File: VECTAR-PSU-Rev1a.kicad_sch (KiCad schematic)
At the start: 63 parts, among them J1 XT60PW-M, J2 XT60PW-M, J3 Conn_01x02_Socket, J5 Conn_01x06_Socket, J6 XT90PW-M, Q1 2N7002, Q2 IRFB7437, Q3 IRFB7437, SW2 RA1113112R, U1 LM74502DDFR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

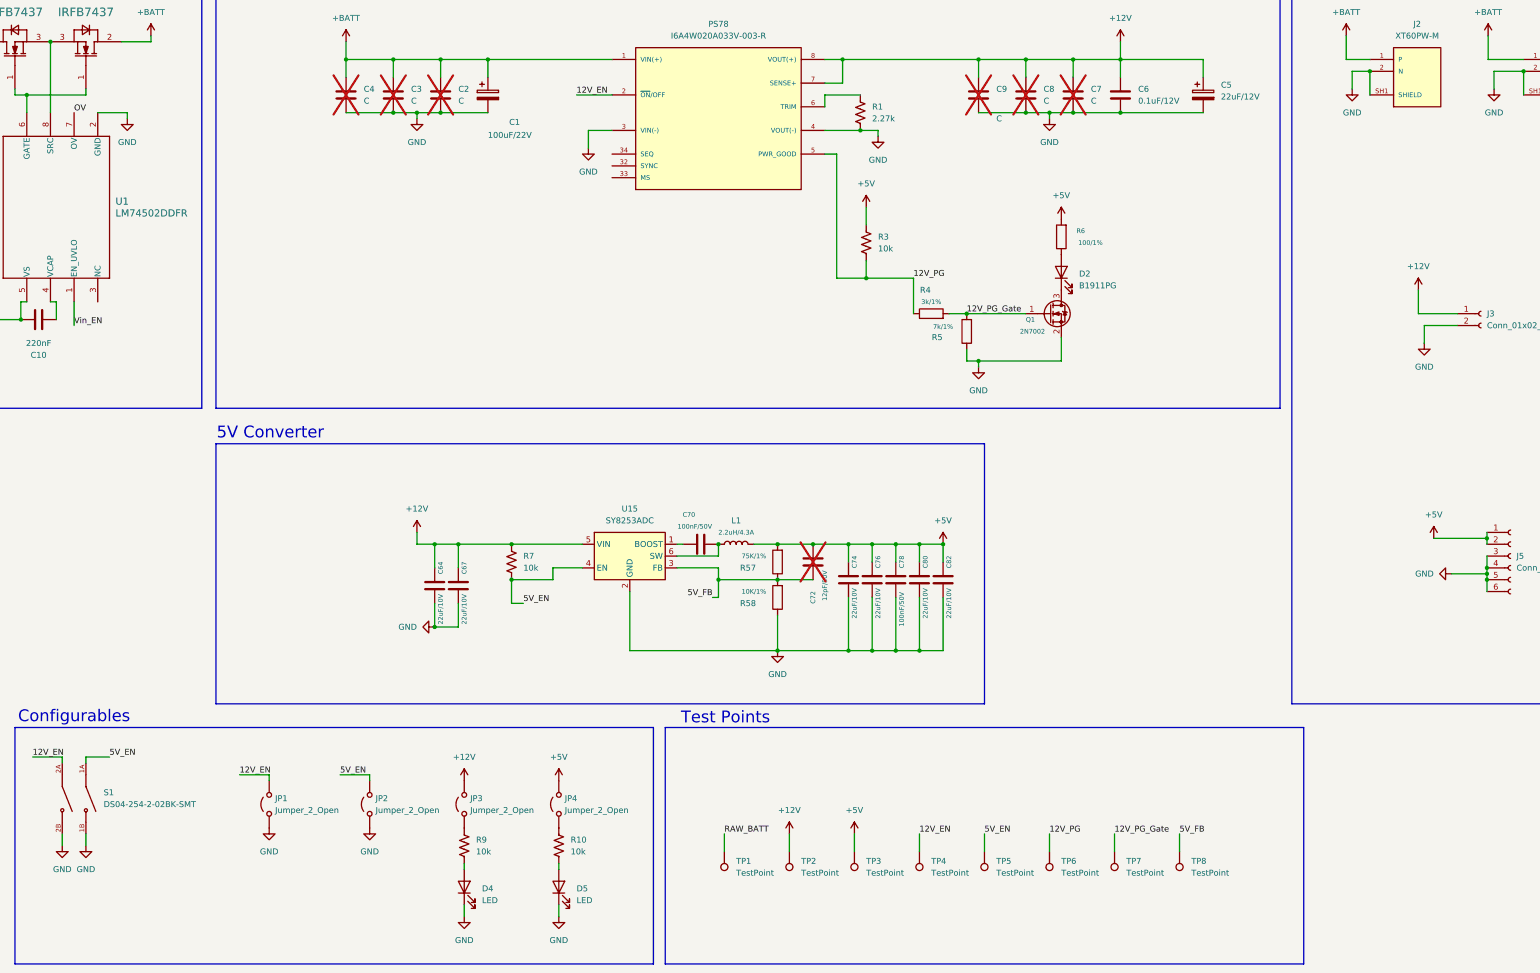
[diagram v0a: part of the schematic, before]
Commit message: schematic complete, adding footprints now
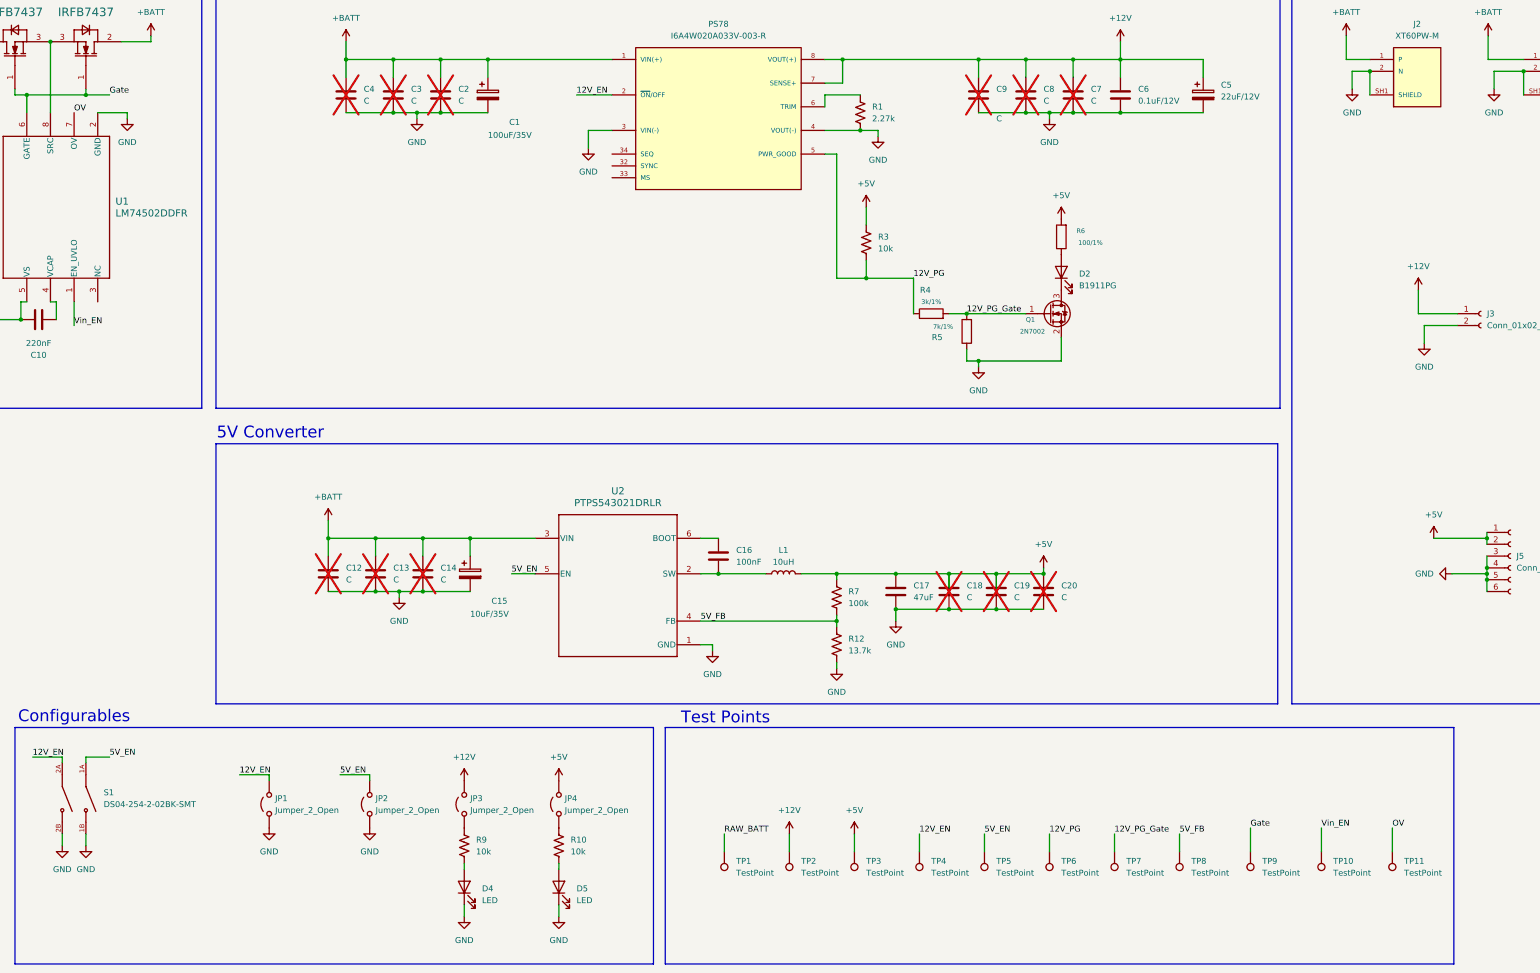
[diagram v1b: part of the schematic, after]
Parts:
- removed C64, C67, C74, C76, C80, C82: 22uF/10V, Capacitor_SMD:C_0603_1608Metric, symbol Device:C
- removed C70, C78: 100nF/50V, Capacitor_SMD:C_0603_1608Metric, symbol Device:C
- removed C72: 12pF/50V, Capacitor_SMD:C_0402_1005Metric, symbol Device:C
- removed R57: 75K/1%, Resistor_SMD:R_0603_1608Metric, symbol Device:R
- removed R58: 10K/1%, Resistor_SMD:R_0603_1608Metric, symbol Device:R
- removed U15: SY8253ADC, symbol Regulator_Switching:LM2734X
- added C12, C13, C14, C18, C19, C20: C, Capacitor_SMD:C_0603_1608Metric, symbol Device:C
- added C15: 10uF/35V, Capacitor_SMD:C_0603_1608Metric, symbol Device:C_Polarized
- added C16: 100nF, Capacitor_SMD:C_0603_1608Metric, symbol Device:C
- added C17: 47uF, PSU-Rev1:CAPAE660X600N, symbol Device:C
- added R12: 13.7k, Resistor_SMD:R_0603_1608Metric, symbol Device:R_US
- added TP10, TP11, TP9: TestPoint, symbol Connector:TestPoint
- added U2: PTPS543021DRLR, PSU-Rev1:DRL0006A-MFG, symbol PSU-Rev1:PTPS543021DRLR
- C1: value 100uF/22V -> 100uF/35V; footprint (none) -> PSU-Rev1:EHBSA035M1010608T
- C5: footprint (none) -> Capacitor_SMD:C_0805_2012Metric
- F1: footprint (none) -> PSU-Rev1:0498150.M
- L1: value 2.2uH/4.3A -> 10uH; footprint (none) -> PSU-Rev1:IND_BOURNS_SDR1307
- Q1: footprint (none) -> PSU-Rev1:SOT95P240X111-3N
- Q2, Q3: footprint (none) -> Resistor_SMD:R_0603_1608Metric
- R7: value 10k -> 100k
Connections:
- net +12V: no longer R7.1
- net +5V: now also R7.1, C17.1, C18.1, C19.1, C20.1
- net +BATT: now also C12.1, C13.1, C14.1, C15.1, U2.3 (VIN)
- net 5V_EN: now also U2.5 (EN); no longer R7.2
- net 5V_FB: now also R7.2, R12.1, U2.4 (FB)
- net GND: now also C12.2, C13.2, C14.2, C15.2, C17.2, C18.2, C19.2, C20.2, R12.2, U2.1 (GND)
- net OV: now also TP11.1
- net Vin_EN: now also TP10.1
- net Gate: now reaches Q2.1 (GATE), Q3.1 (GATE), U1.6 (GATE)
- net Gate: now also TP9.1
- net at L1.1: now also C16.2, U2.2 (SW)
- new net: C16.1, U2.6 (BOOT)

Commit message: schematic complete, layout started
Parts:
- D4: value LED -> Yellow; footprint (none) -> PSU-Rev1:LTST_C190KSKT
- D5: value LED -> Red; footprint (none) -> PSU-Rev1:LTST_S270KRKT
- J3: footprint PSU-Rev1:AMASS_XT60PW-M -> PSU-Rev1:Rocker-Switch
- J5: footprint (none) -> PSU-Rev1:6-pin-connector
- JP1, JP2, JP3, JP4: footprint (none) -> Resistor_SMD:R_0603_1608Metric
- Q2, Q3: footprint Resistor_SMD:R_0603_1608Metric -> PSU-Rev1:TO254P483X1016X1944-3B
- R1: footprint Resistor_SMD:R_0603_1608Metric -> Resistor_SMD:R_0805_2012Metric
- R10: value 10k -> 150
- R9: value 10k -> 500
- SW2: footprint (none) -> PSU-Rev1:Rocker-Switch
- TP1, TP10, TP11, TP2, TP3, TP4, TP5, TP6, TP7, TP8, TP9: footprint (none) -> PSU-Rev1:KEYSTONE_5002
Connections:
- net GND: now also J6.2 (NEG), J6.S1, J6.S2; no longer J6.N (NEG)
- net RAW_BATT: now also J6.1 (POS); no longer J6.P (POS)
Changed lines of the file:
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@@
 	)
 	(junction
+		(at 107.95 88.9)
+		(diameter 0)
+		(color 0 0 0 0)
+	)
+	(junction
 		(at 353.06 203.2)
 		(diameter 0)
@@
 	)
 	(junction
+		(at 93.98 91.44)
+		(diameter 0)
+		(color 0 0 0 0)
+	)
+	(junction
 		(at 102.87 118.11)
 		(diameter 0)
@@
 	(wire
 		(pts
+			(xy 105.41 88.9) (xy 107.95 88.9)
+		)
+		(stroke
+			(width 0)
+			(type default)
+		)
+	)
+	(wire
+		(pts
 			(xy 144.78 92.71) (xy 144.78 96.52)
 		)
@@
 	(wire
 		(pts
+			(xy 90.17 73.66) (xy 90.17 91.44)
+		)
+		(stroke
+			(width 0)
+			(type default)
+		)
+	)
+	(wire
+		(pts
 			(xy 152.4 251.46) (xy 152.4 254)
 		)
@@
 	(wire
 		(pts
+			(xy 90.17 91.44) (xy 93.98 91.44)
+		)
+		(stroke
+			(width 0)
+			(type default)
+		)
+	)
+	(wire
+		(pts
 			(xy 243.84 85.09) (xy 270.51 85.09)
 		)
@@
 	(wire
 		(pts
+			(xy 93.98 91.44) (xy 105.41 91.44)
+		)
+		(stroke
+			(width 0)
+			(type default)
+		)
+	)
+	(wire
+		(pts
 			(xy 350.52 251.46) (xy 350.52 255.27)
 		)
@@
 	(wire
 		(pts
+			(xy 93.98 73.66) (xy 90.17 73.66)
+		)
+		(stroke
+			(width 0)
+			(type default)
+		)
+	)
+	(wire
+		(pts
 			(xy 316.23 100.33) (xy 323.85 100.33)
 		)
@@
 	(wire
 		(pts
+			(xy 105.41 91.44) (xy 105.41 88.9)
+		)
+		(stroke
+			(width 0)
+			(type default)
+		)
+	)
+	(wire
+		(pts
 			(xy 342.9 195.58) (xy 342.9 199.39)
 		)
@@
 			)
 		)
-		(property "Footprint" ""
+		(property "Footprint" "PSU-Rev1:KEYSTONE_5002"
 			(at 373.38 255.27 0)
 			(effects
@@
 			)
 		)
-		(property "Footprint" ""
+		(property "Footprint" "Resistor_SMD:R_0603_1608Metric"
 			(at 218.44 245.11 0)
 			(effects
@@
 			)
 		)
-		(property "Footprint" "Resistor_SMD:R_0603_1608Metric"
+		(property "Footprint" "PSU-Rev1:TO254P483X1016X1944-3B"
 			(at 139.7 86.36 0)
 			(effects
@@
 			)
 		)
-		(property "Footprint" "PSU-Rev1:AMASS_XT60PW-M"
+		(property "Footprint" "PSU-Rev1:Rocker-Switch"
 			(at 457.2 139.7 0)
 			(effects
@@
 			)
 		)
-		(property "Value" "10k"
+		(property "Value" "500"
 			(at 241.3 255.2699 0)
 			(effects
@@
 			)
 		)
-		(property "Footprint" ""
+		(property "Footprint" "Resistor_SMD:R_0603_1608Metric"
 			(at 196.85 245.11 0)
 			(effects
@@
 			)
 		)
-		(property "Value" "10k"
+		(property "Value" "150"
 			(at 261.62 255.2699 0)
 			(effects
@@
 			)
 		)
-		(pin "P"
+		(pin "S1"
+		)
+		(pin "S2"
 		)
-		(pin "N"
+		(pin "1"
+		)
+		(pin "2"
 		)
 		(instances
@@
 			)
 		)
-		(property "Footprint" "Resistor_SMD:R_0603_1608Metric"
+		(property "Footprint" "Resistor_SMD:R_0805_2012Metric"
 			(at 324.866 96.774 90)
 			(effects
@@
 			)
 		)
-		(property "Footprint" ""
+		(property "Footprint" "PSU-Rev1:KEYSTONE_5002"
 			(at 402.59 255.27 0)
 			(effects
@@
 			)
 		)
-		(property "Value" "LED"
+		(property "Value" "Yellow"
 			(at 242.57 265.7474 90)
 			(effects
@@
 			)
 		)
-		(property "Footprint" ""
+		(property "Footprint" "PSU-Rev1:LTST_C190KSKT"
 			(at 238.76 262.89 0)
 			(effects
@@
 			)
 		)
-		(property "Datasheet" "~"
+		(property "Datasheet" "https://optoelectronics.liteon.com/upload/download/DS-22-99-0189/LTST-C190KSKT.pdf"
 			(at 238.76 262.89 0)
 			(effects
@@
 			)
 		)
-		(property "Description" "Light emitting diode"
+		(property "Description" "Yellow light emitting diode"
 			(at 238.76 262.89 0)
 			(effects
@@
 			)
 		)
+		(property "Field6" ""
+			(at 238.76 262.89 90)
+			(effects
+				(font
+					(size 1.27 1.27)
+				)
+				(hide yes)
+			)
+		)
+		(property "Field7" ""
+			(at 238.76 262.89 90)
+			(effects
+				(font
+					(size 1.27 1.27)
+				)
+				(hide yes)
+			)
+		)
+		(property "Field8" ""
+			(at 238.76 262.89 90)
+			(effects
+				(font
+					(size 1.27 1.27)
+				)
+				(hide yes)
+			)
+		)
 		(pin "2"
 		)
@@
 			)
 		)
-		(property "Footprint" ""
+		(property "Footprint" "PSU-Rev1:KEYSTONE_5002"
 			(at 345.44 255.27 0)
 			(effects
@@
 			)
 		)
-		(property "Footprint" ""
+		(property "Footprint" "PSU-Rev1:KEYSTONE_5002"
 			(at 331.47 255.27 0)
 			(effects
@@
 			)
 		)
-		(property "Footprint" ""
+		(property "Footprint" "Resistor_SMD:R_0603_1608Metric"
 			(at 259.08 245.11 0)
 			(effects
@@
 			)
 		)
-		(property "Footprint" ""
+		(property "Footprint" "PSU-Rev1:KEYSTONE_5002"
 			(at 433.07 255.27 0)
 			(effects
@@
 			)
 		)
-		(property "Footprint" "Resistor_SMD:R_0603_1608Metric"
+		(property "Footprint" "PSU-Rev1:TO254P483X1016X1944-3B"
 			(at 160.02 86.36 0)
 			(effects
@@
 			)
 		)
-		(property "Footprint" ""
+		(property "Footprint" "PSU-Rev1:6-pin-connector"
 			(at 463.55 191.77 0)
 			(effects
@@
 			)
 		)
-		(property "Footprint" ""
+		(property "Footprint" "PSU-Rev1:KEYSTONE_5002"
 			(at 303.53 255.27 0)
 			(effects
@@
 			)
 		)
-		(property "Footprint" ""
+		(property "Footprint" "PSU-Rev1:KEYSTONE_5002"
 			(at 387.35 255.27 0)
 			(effects
@@
 			)
 		)
-		(property "Footprint" ""
+		(property "Footprint" "PSU-Rev1:KEYSTONE_5002"
 			(at 359.41 255.27 0)
 			(effects
@@
 			)
 		)
-		(property "Footprint" ""
+		(property "Footprint" "PSU-Rev1:KEYSTONE_5002"
 			(at 289.56 255.27 0)
 			(effects
@@
 			)
 		)
-		(property "Footprint" ""
+		(property "Footprint" "PSU-Rev1:KEYSTONE_5002"
 			(at 417.83 255.27 0)
 			(effects
@@
 			)
 		)
-		(property "Footprint" ""
+		(property "Footprint" "Resistor_SMD:R_0603_1608Metric"
 			(at 238.76 245.11 0)
 			(effects
@@
 			)
 		)
-		(property "Footprint" ""
+		(property "Footprint" "PSU-Rev1:KEYSTONE_5002"
 			(at 317.5 255.27 0)
 			(effects
@@
 			)
 		)
-		(property "Value" "LED"
+		(property "Value" "Red"
 			(at 262.89 265.7474 90)
 			(effects
@@
 			)
 		)
-		(property "Footprint" ""
+		(property "Footprint" "PSU-Rev1:LTST_S270KRKT"
 			(at 259.08 262.89 0)
 			(effects
@@
 			)
 		)
-		(property "Datasheet" "~"
+		(property "Datasheet" "https://optoelectronics.liteon.com/upload/download/DS22-2000-210/LTST-S270KRKT.pdf"
 			(at 259.08 262.89 0)
 			(effects
@@
 			)
 		)
-		(property "Footprint" ""
+		(property "Footprint" "PSU-Rev1:Rocker-Switch"
 			(at 121.92 124.46 0)
 			(effects

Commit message: PCB Rev 1 Complete
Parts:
- added TP12: TestPoint, PSU-Rev1:KEYSTONE_5002, symbol Connector:TestPoint
- F1: footprint PSU-Rev1:0498150.M -> PSU-Rev1:3-140-178
- R1: value 2.27k -> 1.9k
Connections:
- net +12V: now also C12.1, C13.1, C14.1, C15.1, U2.1 (VIN)
- net +BATT: no longer C12.1, C13.1, C14.1, C15.1, U2.3 (VIN)
- net 5V_FB: now also U2.6 (FB); no longer U2.4 (FB)
- net GND: now also U2.3 (GND), TP12.1; no longer U2.1 (GND)
- net at C16.1: now also U2.4 (BOOT); no longer U2.6 (BOOT)
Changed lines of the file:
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@@
 	(rectangle
 		(start 281.94 228.6)
-		(end 451.358 279.4)
+		(end 465.328 279.4)
 		(stroke
 			(width 0)
@@
 	(wire
 		(pts
+			(xy 459.74 245.11) (xy 459.74 246.38)
+		)
+		(stroke
+			(width 0)
+			(type default)
+		)
+	)
+	(wire
+		(pts
 			(xy 359.41 85.09) (xy 349.25 85.09)
 		)
@@
 	(wire
 		(pts
+			(xy 453.39 245.11) (xy 453.39 255.27)
+		)
+		(stroke
+			(width 0)
+			(type default)
+		)
+	)
+	(wire
+		(pts
 			(xy 196.85 240.03) (xy 196.85 238.76)
 		)
@@
 	(wire
 		(pts
+			(xy 453.39 245.11) (xy 459.74 245.11)
+		)
+		(stroke
+			(width 0)
+			(type default)
+		)
+	)
+	(wire
+		(pts
 			(xy 318.77 214.63) (xy 318.77 215.9)
 		)
@@
 	)
 	(symbol
-		(lib_id "power:+BATT")
-		(at 209.55 184.15 0)
-		(unit 1)
-		(exclude_from_sim no)
-		(in_bom yes)
-		(on_board yes)
-		(dnp no)
-		(fields_autoplaced yes)
-		(property "Reference" "#PWR08"
-			(at 209.55 187.96 0)
-			(effects
-				(font
-					(size 1.27 1.27)
-				)
-				(hide yes)
-			)
-		)
-		(property "Value" "+BATT"
-			(at 209.55 179.07 0)
-			(effects
-				(font
-					(size 1.27 1.27)
-				)
-			)
-		)
-		(property "Footprint" ""
-			(at 209.55 184.15 0)
-			(effects
-				(font
-					(size 1.27 1.27)
-				)
-				(hide yes)
-			)
-		)
-		(property "Datasheet" ""
-			(at 209.55 184.15 0)
-			(effects
-				(font
-					(size 1.27 1.27)
-				)
-				(hide yes)
-			)
-		)
-		(property "Description" "Power symbol creates a global label with name \"+BATT\""
-			(at 209.55 184.15 0)
-			(effects
-				(font
-					(size 1.27 1.27)
-				)
-				(hide yes)
-			)
-		)
-		(pin "1"
-		)
-		(instances
-			(project "VECTAR-PSU-Rev1a"
-				(path "/4bea2110-1f4a-4734-955b-ccea5d17fc20"
-					(reference "#PWR08")
-					(unit 1)
-				)
-			)
-		)
-	)
-	(symbol
 		(lib_id "PSU-Rev1:XT60PW-M")
 		(at 443.484 87.63 0)
@@
 	)
 	(symbol
+		(lib_id "power:+12V")
+		(at 209.55 184.15 0)
+		(unit 1)
+		(exclude_from_sim no)
+		(in_bom yes)
+		(on_board yes)
+		(dnp no)
+		(fields_autoplaced yes)
+		(property "Reference" "#PWR08"
+			(at 209.55 187.96 0)
+			(effects
+				(font
+					(size 1.27 1.27)
+				)
+				(hide yes)
+			)
+		)
+		(property "Value" "+12V"
+			(at 209.55 179.07 0)
+			(effects
+				(font
+					(size 1.27 1.27)
+				)
+			)
+		)
+		(property "Footprint" ""
+			(at 209.55 184.15 0)
+			(effects
+				(font
+					(size 1.27 1.27)
+				)
+				(hide yes)
+			)
+		)
+		(property "Datasheet" ""
+			(at 209.55 184.15 0)
+			(effects
+				(font
+					(size 1.27 1.27)
+				)
+				(hide yes)
+			)
+		)
+		(property "Description" "Power symbol creates a global label with name \"+12V\""
+			(at 209.55 184.15 0)
+			(effects
+				(font
+					(size 1.27 1.27)
+				)
+				(hide yes)
+			)
+		)
+		(pin "1"
+		)
+		(instances
+			(project "VECTAR-PSU-Rev1a"
+				(path "/4bea2110-1f4a-4734-955b-ccea5d17fc20"
+					(reference "#PWR08")
+					(unit 1)
+				)
+			)
+		)
+	)
+	(symbol
 		(lib_id "power:GND")
 		(at 218.44 250.19 0)
@@
 			)
 		)
-		(property "Value" "2.27k"
+		(property "Value" "1.9k"
 			(at 326.39 97.7899 0)
 			(effects
@@
 	)
 	(symbol
+		(lib_id "power:GND")
+		(at 459.74 246.38 0)
+		(unit 1)
+		(exclude_from_sim no)
+		(in_bom yes)
+		(on_board yes)
+		(dnp no)
+		(fields_autoplaced yes)
+		(property "Reference" "#PWR034"
+			(at 459.74 252.73 0)
+			(effects
+				(font
+					(size 1.27 1.27)
+				)
+				(hide yes)
+			)
+		)
+		(property "Value" "GND"
+			(at 459.74 251.46 0)
+			(effects
+				(font
+					(size 1.27 1.27)
+				)
+			)
+		)
+		(property "Footprint" ""
+			(at 459.74 246.38 0)
+			(effects
+				(font
+					(size 1.27 1.27)
+				)
+				(hide yes)
+			)
+		)
+		(property "Datasheet" ""
+			(at 459.74 246.38 0)
+			(effects
+				(font
+					(size 1.27 1.27)
+				)
+				(hide yes)
+			)
+		)
+		(property "Description" ""
+			(at 459.74 246.38 0)
+			(effects
+				(font
+					(size 1.27 1.27)
+				)
+				(hide yes)
+			)
+		)
+		(pin "1"
+		)
+		(instances
+			(project "VECTAR-PSU-Rev1a"
+				(path "/4bea2110-1f4a-4734-955b-ccea5d17fc20"
+					(reference "#PWR034")
+					(unit 1)
+				)
+			)
+		)
+	)
+	(symbol
 		(lib_id "power:+5V")
 		(at 259.08 240.03 0)
@@
 	(symbol
 		(lib_id "Connector:TestPoint")
+		(at 453.39 255.27 180)
+		(unit 1)
+		(exclude_from_sim no)
+		(in_bom yes)
+		(on_board yes)
+		(dnp no)
+		(fields_autoplaced yes)
+		(property "Reference" "TP12"
+			(at 455.93 257.3019 0)
+			(effects
+				(font
+					(size 1.27 1.27)
+				)
+				(justify right)
+			)
+		)
+		(property "Value" "TestPoint"
+			(at 455.93 259.8419 0)
+			(effects
+				(font
+					(size 1.27 1.27)
+				)
+				(justify right)
+			)
+		)
+		(property "Footprint" "PSU-Rev1:KEYSTONE_5002"
+			(at 448.31 255.27 0)
+			(effects
+				(font
+					(size 1.27 1.27)
+				)
+				(hide yes)
+			)
+		)
+		(property "Datasheet" "~"
+			(at 448.31 255.27 0)
+			(effects
+				(font
+					(size 1.27 1.27)
+				)
+				(hide yes)
+			)
+		)
+		(property "Description" "test point"
+			(at 453.39 255.27 0)
+			(effects
+				(font
+					(size 1.27 1.27)
+				)
+				(hide yes)
+			)
+		)
+		(pin "1"
+		)
+		(instances
+			(project "VECTAR-PSU-Rev1a"
+				(path "/4bea2110-1f4a-4734-955b-ccea5d17fc20"
+					(reference "TP12")
+					(unit 1)
+				)
+			)
+		)
+	)
+	(symbol
+		(lib_id "Connector:TestPoint")
 		(at 364.49 255.27 180)
 		(unit 1)
@@
 			)
 		)
-		(property "Footprint" "PSU-Rev1:0498150.M"
+		(property "Footprint" "PSU-Rev1:3-140-178"
 			(at 120.65 83.058 90)
 			(effects
@@
 			)
 		)
-		(property "Datasheet" "~"
+		(property "Datasheet" "https://www.schurter.com/en/datasheet/typ_UHS.pdf"
 			(at 120.65 81.28 0)
 			(effects

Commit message: PCB Rev 1 Ordered
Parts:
- R1: value 1.9k -> 1.89k
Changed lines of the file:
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@@
 			)
 		)
-		(property "Value" "1.9k"
+		(property "Value" "1.89k"
 			(at 326.39 97.7899 0)
 			(effects
